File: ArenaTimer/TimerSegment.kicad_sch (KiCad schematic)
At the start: 8 parts

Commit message: added digits
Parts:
- renumbered C253 to C173, C254 to C174, C255 to C175, C256 to C176, D253 to D173, D254 to D174, D255 to D175, D256 to D176
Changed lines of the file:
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@@
 		(on_board yes)
 		(dnp no)
-		(property "Reference" "#PWR0765"
+		(property "Reference" "#PWR0525"
 			(at 167.64 95.25 0)
 			(effects
@@
 		(on_board yes)
 		(dnp no)
-		(property "Reference" "#PWR0761"
+		(property "Reference" "#PWR0521"
 			(at 130.81 115.57 0)
 			(effects
@@
 		(on_board yes)
 		(dnp no)
-		(property "Reference" "#PWR0767"
+		(property "Reference" "#PWR0527"
 			(at 187.96 115.57 0)
 			(effects
@@
 		(dnp no)
 		(fields_autoplaced yes)
-		(property "Reference" "#PWR0763"
+		(property "Reference" "#PWR0523"
 			(at 160.02 81.28 0)
 			(effects
@@
 		(dnp no)
 		(fields_autoplaced yes)
-		(property "Reference" "#PWR0766"
+		(property "Reference" "#PWR0526"
 			(at 187.96 81.28 0)
 			(effects
@@
 		(dnp no)
 		(fields_autoplaced yes)
-		(property "Reference" "#PWR0757"
+		(property "Reference" "#PWR0517"
 			(at 102.87 81.28 0)
 			(effects
@@
 		(dnp no)
 		(fields_autoplaced yes)
-		(property "Reference" "C254"
+		(property "Reference" "C174"
 			(at 142.24 82.5499 0)
 			(effects
@@
 		(dnp no)
 		(fields_autoplaced yes)
-		(property "Reference" "D253"
+		(property "Reference" "D173"
 			(at 114.3 94.0114 0)
 			(effects
@@
 		(dnp no)
 		(fields_autoplaced yes)
-		(property "Reference" "D256"
+		(property "Reference" "D176"
 			(at 199.39 94.0114 0)
 			(effects
@@
 		(dnp no)
 		(fields_autoplaced yes)
-		(property "Reference" "D255"
+		(property "Reference" "D175"
 			(at 171.45 94.0114 0)
 			(effects
@@
 		(dnp no)
 		(fields_autoplaced yes)
-		(property "Reference" "C256"
+		(property "Reference" "C176"
 			(at 199.39 82.5499 0)
 			(effects
@@
 		(dnp no)
 		(fields_autoplaced yes)
-		(property "Reference" "D254"
+		(property "Reference" "D174"
 			(at 142.24 94.0114 0)
 			(effects
@@
 		(dnp no)
 		(fields_autoplaced yes)
-		(property "Reference" "C255"
+		(property "Reference" "C175"
 			(at 171.45 82.5499 0)
 			(effects
@@
 		(dnp no)
 		(fields_autoplaced yes)
-		(property "Reference" "C253"
+		(property "Reference" "C173"
 			(at 114.3 82.5499 0)
 			(effects
@@
 		(on_board yes)
 		(dnp no)
-		(property "Reference" "#PWR0758"
+		(property "Reference" "#PWR0518"
 			(at 102.87 115.57 0)
 			(effects
@@
 		(on_board yes)
 		(dnp no)
-		(property "Reference" "#PWR0759"
+		(property "Reference" "#PWR0519"
 			(at 110.49 95.25 0)
 			(effects
@@
 		(on_board yes)
 		(dnp no)
-		(property "Reference" "#PWR0768"
+		(property "Reference" "#PWR0528"
 			(at 195.58 95.25 0)
 			(effects
@@
 		(on_board yes)
 		(dnp no)
-		(property "Reference" "#PWR0762"
+		(property "Reference" "#PWR0522"
 			(at 138.43 95.25 0)
 			(effects
@@
 		(dnp no)
 		(fields_autoplaced yes)
-		(property "Reference" "#PWR0760"
+		(property "Reference" "#PWR0520"
 			(at 130.81 81.28 0)
 			(effects
@@
 		(on_board yes)
 		(dnp no)
-		(property "Reference" "#PWR0764"
+		(property "Reference" "#PWR0524"
 			(at 160.02 115.57 0)
 			(effects

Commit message: finish up routing
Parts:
- removed C173, C174, C175, C176: 100nF, symbol Device:C
- added D74, D75, D76: WS2812B, LED_SMD:LED_WS2812B_PLCC4_5.0x5.0mm_P3.2mm, symbol LED:WS2812B
- renumbered D173 to D287, D174 to D288, D175 to D289, D176 to D290
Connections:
- net +5V: now also D74.1 (VDD), D75.1 (VDD), D76.1 (VDD)
- net DOUT: now also D76.2 (DOUT); no longer D290.2 (DOUT)
- net GND: now also D74.3 (VSS), D75.3 (VSS), D76.3 (VSS)
- new net: D75.2 (DOUT), D76.4 (DIN)
- new net: D290.2 (DOUT), D74.4 (DIN)
- new net: D74.2 (DOUT), D75.4 (DIN)
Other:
- moved on the sheet: D287, D288, D289, D290

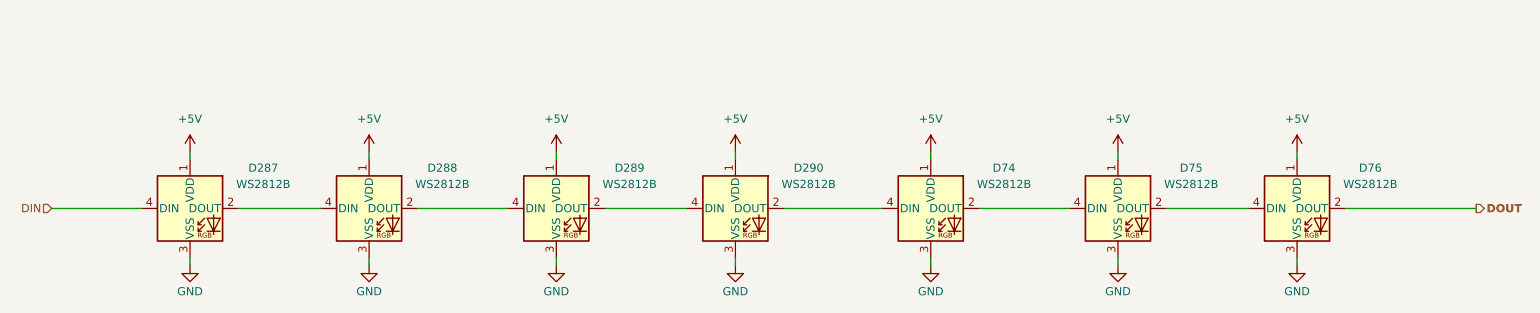
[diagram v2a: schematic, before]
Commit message: add 3d models
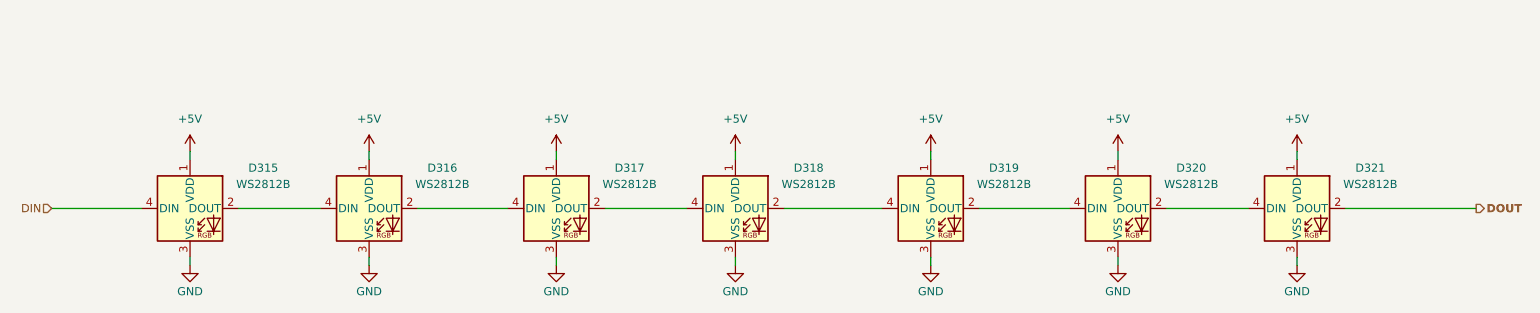
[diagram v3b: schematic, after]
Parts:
- renumbered D287 to D315, D288 to D316, D289 to D317, D290 to D318, D74 to D319, D75 to D320, D76 to D321
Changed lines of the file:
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@@
 		(dnp no)
 		(fields_autoplaced yes)
-		(property "Reference" "D76"
+		(property "Reference" "D321"
 			(at 241.3 95.2814 0)
 			(effects
@@
 		(on_board yes)
 		(dnp no)
-		(property "Reference" "#PWR0152"
+		(property "Reference" "#PWR0642"
 			(at 229.87 116.84 0)
 			(effects
@@
 		(on_board yes)
 		(dnp no)
-		(property "Reference" "#PWR0148"
+		(property "Reference" "#PWR0638"
 			(at 172.72 116.84 0)
 			(effects
@@
 		(on_board yes)
 		(dnp no)
-		(property "Reference" "#PWR0576"
+		(property "Reference" "#PWR0632"
 			(at 85.09 116.84 0)
 			(effects
@@
 		(on_board yes)
 		(dnp no)
-		(property "Reference" "#PWR0580"
+		(property "Reference" "#PWR0636"
 			(at 142.24 116.84 0)
 			(effects
@@
 		(dnp no)
 		(fields_autoplaced yes)
-		(property "Reference" "#PWR0577"
+		(property "Reference" "#PWR0633"
 			(at 114.3 96.52 0)
 			(effects
@@
 		(dnp no)
 		(fields_autoplaced yes)
-		(property "Reference" "#PWR0579"
+		(property "Reference" "#PWR0635"
 			(at 142.24 96.52 0)
 			(effects
@@
 		(dnp no)
 		(fields_autoplaced yes)
-		(property "Reference" "#PWR0147"
+		(property "Reference" "#PWR0637"
 			(at 172.72 96.52 0)
 			(effects
@@
 		(dnp no)
 		(fields_autoplaced yes)
-		(property "Reference" "#PWR0573"
+		(property "Reference" "#PWR0629"
 			(at 57.15 96.52 0)
 			(effects
@@
 		(dnp no)
 		(fields_autoplaced yes)
-		(property "Reference" "#PWR0151"
+		(property "Reference" "#PWR0641"
 			(at 229.87 96.52 0)
 			(effects
@@
 		(dnp no)
 		(fields_autoplaced yes)
-		(property "Reference" "D287"
+		(property "Reference" "D315"
 			(at 68.58 95.2814 0)
 			(effects
@@
 		(dnp no)
 		(fields_autoplaced yes)
-		(property "Reference" "D290"
+		(property "Reference" "D318"
 			(at 153.67 95.2814 0)
 			(effects
@@
 		(dnp no)
 		(fields_autoplaced yes)
-		(property "Reference" "D289"
+		(property "Reference" "D317"
 			(at 125.73 95.2814 0)
 			(effects
@@
 		(dnp no)
 		(fields_autoplaced yes)
-		(property "Reference" "D288"
+		(property "Reference" "D316"
 			(at 96.52 95.2814 0)
 			(effects
@@
 		(on_board yes)
 		(dnp no)
-		(property "Reference" "#PWR0150"
+		(property "Reference" "#PWR0640"
 			(at 201.93 116.84 0)
 			(effects
@@
 		(on_board yes)
 		(dnp no)
-		(property "Reference" "#PWR0574"
+		(property "Reference" "#PWR0630"
 			(at 57.15 116.84 0)
 			(effects
@@
 		(dnp no)
 		(fields_autoplaced yes)
-		(property "Reference" "D74"
+		(property "Reference" "D319"
 			(at 184.15 95.2814 0)
 			(effects
@@
 		(dnp no)
 		(fields_autoplaced yes)
-		(property "Reference" "#PWR0149"
+		(property "Reference" "#PWR0639"
 			(at 201.93 96.52 0)
 			(effects
@@
 		(dnp no)
 		(fields_autoplaced yes)
-		(property "Reference" "#PWR0575"
+		(property "Reference" "#PWR0631"
 			(at 85.09 96.52 0)
 			(effects
@@
 		(dnp no)
 		(fields_autoplaced yes)
-		(property "Reference" "D75"
+		(property "Reference" "D320"
 			(at 213.36 95.2814 0)
 			(effects
@@
 		(on_board yes)
 		(dnp no)
-		(property "Reference" "#PWR0578"
+		(property "Reference" "#PWR0634"
 			(at 114.3 116.84 0)
 			(effects

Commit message: PCB changes, code for TRC timers
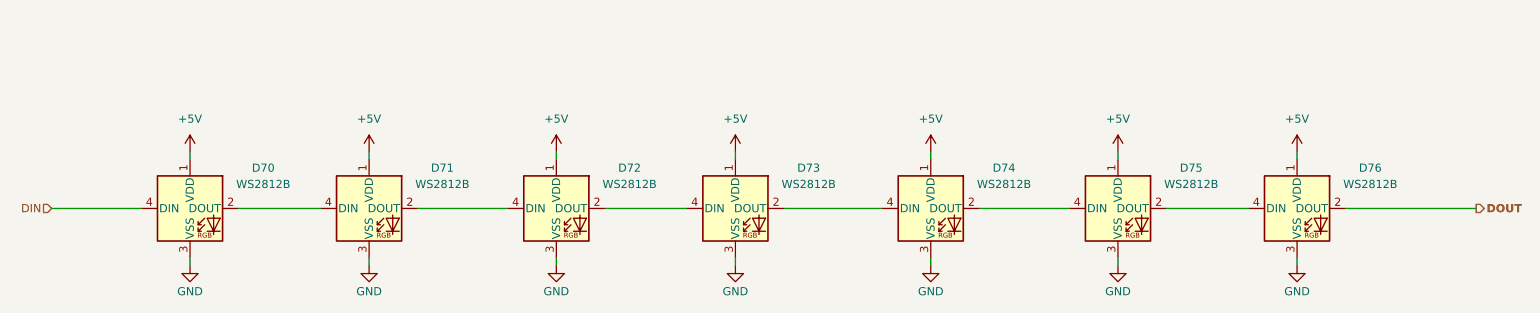
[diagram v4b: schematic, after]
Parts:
- renumbered D315 to D70, D316 to D71, D317 to D72, D318 to D73, D319 to D74, D320 to D75, D321 to D76
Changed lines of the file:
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@@
 (kicad_sch
-	(version 20231120)
+	(version 20250114)
 	(generator "eeschema")
-	(generator_version "8.0")
+	(generator_version "9.0")
 	(paper "A4")
 	(wire
@@
 		(shape output)
 		(at 257.81 101.6 0)
-		(fields_autoplaced yes)
 		(effects
 			(font
@@
 		(shape input)
 		(at 35.56 101.6 180)
-		(fields_autoplaced yes)
 		(effects
 			(font
@@
 		(dnp no)
 		(fields_autoplaced yes)
-		(property "Reference" "D321"
+		(property "Reference" "D76"
 			(at 241.3 95.2814 0)
 			(effects
@@
 		(on_board yes)
 		(dnp no)
-		(property "Reference" "#PWR0642"
+		(property "Reference" "#PWR0152"
 			(at 229.87 116.84 0)
 			(effects
@@
 		(on_board yes)
 		(dnp no)
-		(property "Reference" "#PWR0638"
+		(property "Reference" "#PWR0148"
 			(at 172.72 116.84 0)
 			(effects
@@
 		(on_board yes)
 		(dnp no)
-		(property "Reference" "#PWR0632"
+		(property "Reference" "#PWR0142"
 			(at 85.09 116.84 0)
 			(effects
@@
 		(on_board yes)
 		(dnp no)
-		(property "Reference" "#PWR0636"
+		(property "Reference" "#PWR0146"
 			(at 142.24 116.84 0)
 			(effects
@@
 		(dnp no)
 		(fields_autoplaced yes)
-		(property "Reference" "#PWR0633"
+		(property "Reference" "#PWR0143"
 			(at 114.3 96.52 0)
 			(effects
@@
 		(dnp no)
 		(fields_autoplaced yes)
-		(property "Reference" "#PWR0635"
+		(property "Reference" "#PWR0145"
 			(at 142.24 96.52 0)
 			(effects
@@
 		(dnp no)
 		(fields_autoplaced yes)
-		(property "Reference" "#PWR0637"
+		(property "Reference" "#PWR0147"
 			(at 172.72 96.52 0)
 			(effects
@@
 		(dnp no)
 		(fields_autoplaced yes)
-		(property "Reference" "#PWR0629"
+		(property "Reference" "#PWR0139"
 			(at 57.15 96.52 0)
 			(effects
@@
 		(dnp no)
 		(fields_autoplaced yes)
-		(property "Reference" "#PWR0641"
+		(property "Reference" "#PWR0151"
 			(at 229.87 96.52 0)
 			(effects
@@
 		(dnp no)
 		(fields_autoplaced yes)
-		(property "Reference" "D315"
+		(property "Reference" "D70"
 			(at 68.58 95.2814 0)
 			(effects
@@
 		(dnp no)
 		(fields_autoplaced yes)
-		(property "Reference" "D318"
+		(property "Reference" "D73"
 			(at 153.67 95.2814 0)
 			(effects
@@
 		(dnp no)
 		(fields_autoplaced yes)
-		(property "Reference" "D317"
+		(property "Reference" "D72"
 			(at 125.73 95.2814 0)
 			(effects
@@
 		(dnp no)
 		(fields_autoplaced yes)
-		(property "Reference" "D316"
+		(property "Reference" "D71"
 			(at 96.52 95.2814 0)
 			(effects
@@
 		(on_board yes)
 		(dnp no)
-		(property "Reference" "#PWR0640"
+		(property "Reference" "#PWR0150"
 			(at 201.93 116.84 0)
 			(effects
@@
 		(on_board yes)
 		(dnp no)
-		(property "Reference" "#PWR0630"
+		(property "Reference" "#PWR0140"
 			(at 57.15 116.84 0)
 			(effects
@@
 		(dnp no)
 		(fields_autoplaced yes)
-		(property "Reference" "D319"
+		(property "Reference" "D74"
 			(at 184.15 95.2814 0)
 			(effects
@@
 		(dnp no)
 		(fields_autoplaced yes)
-		(property "Reference" "#PWR0639"
+		(property "Reference" "#PWR0149"
 			(at 201.93 96.52 0)
 			(effects
@@
 		(dnp no)
 		(fields_autoplaced yes)
-		(property "Reference" "#PWR0631"
+		(property "Reference" "#PWR0141"
 			(at 85.09 96.52 0)
 			(effects
@@
 		(dnp no)
 		(fields_autoplaced yes)
-		(property "Reference" "D320"
+		(property "Reference" "D75"
 			(at 213.36 95.2814 0)
 			(effects
@@
 		(on_board yes)
 		(dnp no)
-		(property "Reference" "#PWR0634"
+		(property "Reference" "#PWR0144"
 			(at 114.3 116.84 0)
 			(effects
